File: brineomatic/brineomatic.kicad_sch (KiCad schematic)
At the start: 9 parts, among them U1 ESP32-S3-DEVKITC

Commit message: first pass fully routed
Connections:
- net +3.3V: no longer R17.2
- net GND: now also R17.2
- net Piezo/PIEZO: now also U1.20 (GPIO14); no longer U1.10 (GPIO17)
- net Servos/SERVO1: now also U1.36 (GPIO39); no longer U1.34 (GPIO37)
- net Servos/SERVO2: now also U1.34 (GPIO37); no longer U1.36 (GPIO39)
- net Stepper Driver/DIAG: now also U1.39 (GPIO42); no longer U1.38 (GPIO41)
- net Stepper Driver/DIR: now also U1.41 (GPIO1); no longer U1.40 (GPIO2)
- net Stepper Driver/EN: now also U1.38 (GPIO41); no longer U1.39 (GPIO42)
- net Stepper Driver/STEP: now also U1.40 (GPIO2); no longer U1.41 (GPIO1)
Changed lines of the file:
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@@
 	)
 	(junction
+		(at 270.51 53.34)
+		(diameter 0)
+		(color 0 0 0 0)
+	)
+	(junction
 		(at 180.34 114.3)
 		(diameter 0)
@@
 	)
 	(no_connect
-		(at 161.29 99.06)
-	)
-	(no_connect
 		(at 161.29 88.9)
 	)
@@
 	)
 	(no_connect
+		(at 161.29 76.2)
+	)
+	(no_connect
 		(at 161.29 58.42)
 	)
@@
 	(wire
 		(pts
-			(xy 209.55 43.18) (xy 237.49 43.18)
+			(xy 214.63 48.26) (xy 237.49 48.26)
 		)
 		(stroke
@@
 	(wire
 		(pts
-			(xy 59.69 78.74) (xy 64.77 78.74)
+			(xy 135.89 105.41) (xy 130.81 105.41)
 		)
 		(stroke
@@
 	(wire
 		(pts
-			(xy 33.02 162.56) (xy 39.37 162.56)
+			(xy 59.69 78.74) (xy 64.77 78.74)
 		)
 		(stroke
@@
 	(wire
 		(pts
-			(xy 199.39 78.74) (xy 214.63 78.74)
+			(xy 33.02 162.56) (xy 39.37 162.56)
 		)
 		(stroke
@@
 	(wire
 		(pts
-			(xy 257.81 53.34) (xy 261.62 53.34)
+			(xy 199.39 78.74) (xy 214.63 78.74)
 		)
 		(stroke
@@
 	(wire
 		(pts
-			(xy 201.93 104.14) (xy 199.39 104.14)
+			(xy 257.81 53.34) (xy 261.62 53.34)
 		)
 		(stroke
@@
 	(wire
 		(pts
-			(xy 214.63 48.26) (xy 237.49 48.26)
+			(xy 201.93 104.14) (xy 199.39 104.14)
 		)
 		(stroke
@@
 	(wire
 		(pts
-			(xy 130.81 73.66) (xy 161.29 73.66)
+			(xy 217.17 76.2) (xy 217.17 74.93)
 		)
 		(stroke
@@
 	(wire
 		(pts
-			(xy 217.17 76.2) (xy 217.17 74.93)
+			(xy 180.34 118.11) (xy 180.34 114.3)
 		)
 		(stroke
@@
 	(wire
 		(pts
-			(xy 180.34 118.11) (xy 180.34 114.3)
+			(xy 201.93 101.6) (xy 201.93 104.14)
 		)
 		(stroke
@@
 	(wire
 		(pts
-			(xy 201.93 101.6) (xy 201.93 104.14)
+			(xy 39.37 152.4) (xy 39.37 162.56)
 		)
 		(stroke
@@
 	(wire
 		(pts
-			(xy 39.37 152.4) (xy 39.37 162.56)
+			(xy 135.89 99.06) (xy 135.89 105.41)
 		)
 		(stroke
@@
 	(wire
 		(pts
-			(xy 212.09 45.72) (xy 237.49 45.72)
+			(xy 214.63 88.9) (xy 214.63 92.71)
 		)
 		(stroke
@@
 	(wire
 		(pts
-			(xy 214.63 88.9) (xy 214.63 92.71)
+			(xy 157.48 68.58) (xy 161.29 68.58)
 		)
 		(stroke
@@
 	(wire
 		(pts
-			(xy 157.48 68.58) (xy 161.29 68.58)
+			(xy 212.09 45.72) (xy 237.49 45.72)
 		)
 		(stroke
@@
 	(wire
 		(pts
-			(xy 217.17 52.07) (xy 237.49 52.07)
-		)
-		(stroke
-			(width 0)
-			(type default)
-		)
-	)
-	(wire
-		(pts
 			(xy 209.55 58.42) (xy 209.55 43.18)
 		)
@@
 	(wire
 		(pts
-			(xy 217.17 52.07) (xy 217.17 66.04)
+			(xy 217.17 50.8) (xy 217.17 66.04)
 		)
 		(stroke
@@
 	(wire
 		(pts
-			(xy 130.81 97.79) (xy 132.08 97.79)
+			(xy 217.17 50.8) (xy 237.49 50.8)
 		)
 		(stroke
@@
 	(wire
 		(pts
-			(xy 33.02 130.81) (xy 39.37 130.81)
+			(xy 130.81 97.79) (xy 132.08 97.79)
 		)
 		(stroke
@@
 	(wire
 		(pts
-			(xy 39.37 142.24) (xy 39.37 152.4)
+			(xy 33.02 130.81) (xy 39.37 130.81)
 		)
 		(stroke
@@
 	(wire
 		(pts
-			(xy 270.51 41.91) (xy 270.51 44.45)
+			(xy 39.37 142.24) (xy 39.37 152.4)
 		)
 		(stroke
@@
 	(wire
 		(pts
+			(xy 209.55 43.18) (xy 237.49 43.18)
+		)
+		(stroke
+			(width 0)
+			(type default)
+		)
+	)
+	(wire
+		(pts
+			(xy 161.29 99.06) (xy 135.89 99.06)
+		)
+		(stroke
+			(width 0)
+			(type default)
+		)
+	)
+	(wire
+		(pts
 			(xy 39.37 130.81) (xy 39.37 142.24)
 		)
@@
 		)
 	)
+	(wire
+		(pts
+			(xy 270.51 44.45) (xy 270.51 53.34)
+		)
+		(stroke
+			(width 0)
+			(type default)
+		)
+	)
 	(global_label "ADC_ALERT{slash}RDY"
 		(shape input)
@@
 	)
 	(symbol
-		(lib_id "power:+3.3V")
-		(at 270.51 41.91 0)
-		(unit 1)
-		(exclude_from_sim no)
-		(in_bom yes)
-		(on_board yes)
-		(dnp no)
-		(fields_autoplaced yes)
-		(property "Reference" "#PWR046"
-			(at 270.51 45.72 0)
-			(effects
-				(font
-					(size 1.27 1.27)
-				)
-				(hide yes)
-			)
-		)
-		(property "Value" "+3.3V"
-			(at 273.05 40.6399 0)
-			(effects
-				(font
-					(size 1.27 1.27)
-				)
-				(justify left)
-			)
-		)
-		(property "Footprint" ""
-			(at 270.51 41.91 0)
-			(effects
-				(font
-					(size 1.27 1.27)
-				)
-				(hide yes)
-			)
-		)
-		(property "Datasheet" ""
-			(at 270.51 41.91 0)
-			(effects
-				(font
-					(size 1.27 1.27)
-				)
-				(hide yes)
-			)
-		)
-		(property "Description" "Power symbol creates a global label with name \"+3.3V\""
-			(at 270.51 41.91 0)
-			(effects
-				(font
-					(size 1.27 1.27)
-				)
-				(hide yes)
-			)
-		)
-		(pin "1"
-		)
-		(instances
-			(project "brineomatic"
-				(path "/96477ae2-ef08-48f3-8dd4-fe4478541f68"
-					(reference "#PWR046")
-					(unit 1)
-				)
-			)
-		)
-	)
-	(symbol
 		(lib_id "power:GND")
 		(at 270.51 55.88 0)
@@
 		)
 		(pin "SERVO1" input
-			(at 222.25 74.93 180)
+			(at 222.25 72.39 180)
 			(effects
 				(font
@@
 		)
 		(pin "SERVO2" input
-			(at 222.25 72.39 180)
+			(at 222.25 74.93 180)
 			(effects
 				(font
@@
 		)
 		(pin "DIR" input
-			(at 237.49 45.72 180)
+			(at 237.49 43.18 180)
 			(effects
 				(font
@@
 		)
 		(pin "EN" input
-			(at 237.49 48.26 180)
+			(at 237.49 50.8 180)
 			(effects
 				(font
@@
 		)
 		(pin "STEP" input
-			(at 237.49 43.18 180)
+			(at 237.49 45.72 180)
 			(effects
 				(font
@@
 		)
 		(pin "DIAG" input
-			(at 237.49 52.07 180)
+			(at 237.49 48.26 180)
 			(effects
 				(font
@@
 	)
 	(sheet
-		(at 111.76 71.12)
-		(size 19.05 3.81)
-		(exclude_from_sim no)
-		(in_bom yes)
-		(on_board yes)
-		(dnp no)
-		(fields_autoplaced yes)
-		(stroke
-			(width 0.1524)
-			(type solid)
-		)
-		(fill
-			(color 0 0 0 0.0000)
-		)
-		(property "Sheetname" "Piezo"
-			(at 111.76 70.4084 0)
-			(effects
-				(font
-					(size 1.27 1.27)
-				)
-				(justify left bottom)
-			)
-		)
-		(property "Sheetfile" "piezo.kicad_sch"
-			(at 111.76 75.5146 0)
-			(effects
-				(font
-					(size 1.27 1.27)
-				)
-				(justify left top)
-				(hide yes)
-			)
-		)
-		(pin "PIEZO" input
-			(at 130.81 73.66 0)
-			(effects
-				(font
-					(size 1.27 1.27)
-				)
-				(justify right)
-			)
-		)
-		(instances
-			(project "brineomatic"
-				(path "/96477ae2-ef08-48f3-8dd4-fe4478541f68"
-					(page "16")
-				)
-			)
-		)
-	)
-	(sheet
 		(at 222.25 107.95)
 		(size 31.75 5.08)
@@
 				)
 			)
+		)
+	)
+	(sheet
+		(at 111.76 102.87)
+		(size 19.05 3.81)
+		(exclude_from_sim no)
+		(in_bom yes)
+		(on_board yes)
+		(dnp no)
+		(fields_autoplaced yes)
+		(stroke
+			(width 0.1524)
+			(type solid)
+		)
+		(fill
+			(color 0 0 0 0.0000)
+		)
+		(property "Sheetname" "Piezo"
+			(at 111.76 102.1584 0)
+			(effects
+				(font
+					(size 1.27 1.27)
+				)
+				(justify left bottom)
+			)
+		)
+		(property "Sheetfile" "piezo.kicad_sch"
+			(at 111.76 107.2646 0)
+			(effects
+				(font
+					(size 1.27 1.27)
+				)
+				(justify left top)
+				(hide yes)
+			)
+		)
+		(pin "PIEZO" input
+			(at 130.81 105.41 0)
+			(effects
+				(font
+					(size 1.27 1.27)
+				)
+				(justify right)
+			)
+		)
+		(instances
+			(project "brineomatic"
+				(path "/96477ae2-ef08-48f3-8dd4-fe4478541f68"
+					(page "9")
+				)
+			)

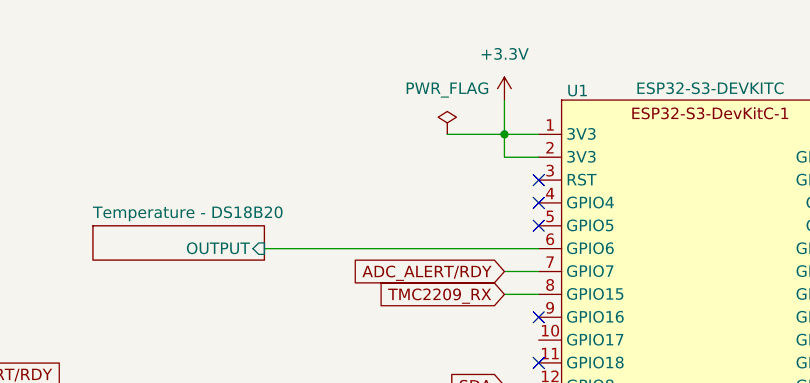
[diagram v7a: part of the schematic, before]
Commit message: added fuse on 3.3v
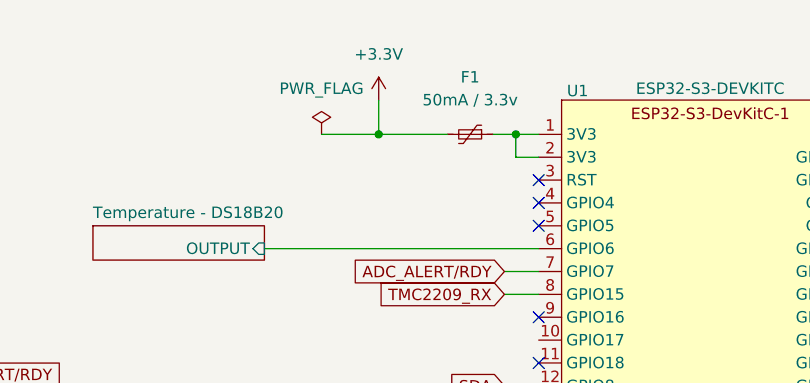
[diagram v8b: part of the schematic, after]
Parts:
- added F1: 50mA / 3.3v, Fuse:Fuse_0603_1608Metric, symbol Device:Polyfuse_Small
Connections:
- net +3.3V: now also F1.2; no longer U1.1 (3V3), U1.2 (3V3)
- new net: F1.1, U1.1 (3V3), U1.2 (3V3)
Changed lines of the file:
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@@
+	)
+	(junction
+		(at 158.75 50.8)
+		(diameter 0)
+		(color 0 0 0 0)
 	)
 	(junction
@@
 	)
 	(junction
-		(at 157.48 50.8)
+		(at 143.51 50.8)
 		(diameter 0)
 		(color 0 0 0 0)
@@
 	(wire
 		(pts
-			(xy 151.13 50.8) (xy 157.48 50.8)
+			(xy 137.16 50.8) (xy 143.51 50.8)
 		)
 		(stroke
@@
 	(wire
 		(pts
-			(xy 161.29 53.34) (xy 157.48 53.34)
-		)
-		(stroke
-			(width 0)
-			(type default)
-		)
-	)
-	(wire
-		(pts
 			(xy 62.23 73.66) (xy 62.23 59.69)
 		)
@@
 	(wire
 		(pts
+			(xy 156.21 50.8) (xy 158.75 50.8)
+		)
+		(stroke
+			(width 0)
+			(type default)
+		)
+	)
+	(wire
+		(pts
 			(xy 214.63 63.5) (xy 214.63 48.26)
 		)
@@
 	(wire
 		(pts
+			(xy 158.75 53.34) (xy 158.75 50.8)
+		)
+		(stroke
+			(width 0)
+			(type default)
+		)
+	)
+	(wire
+		(pts
 			(xy 257.81 53.34) (xy 261.62 53.34)
 		)
@@
 	(wire
 		(pts
+			(xy 158.75 50.8) (xy 161.29 50.8)
+		)
+		(stroke
+			(width 0)
+			(type default)
+		)
+	)
+	(wire
+		(pts
 			(xy 93.98 74.93) (xy 93.98 68.58)
 		)
@@
 	(wire
 		(pts
-			(xy 157.48 50.8) (xy 157.48 53.34)
-		)
-		(stroke
-			(width 0)
-			(type default)
-		)
-	)
-	(wire
-		(pts
 			(xy 217.17 72.39) (xy 217.17 71.12)
 		)
@@
 	(wire
 		(pts
-			(xy 157.48 46.99) (xy 157.48 50.8)
+			(xy 143.51 46.99) (xy 143.51 50.8)
 		)
 		(stroke
@@
 	(wire
 		(pts
-			(xy 157.48 50.8) (xy 161.29 50.8)
+			(xy 143.51 50.8) (xy 151.13 50.8)
 		)
 		(stroke
@@
 		(pts
 			(xy 158.75 104.14) (xy 158.75 114.3)
+		)
+		(stroke
+			(width 0)
+			(type default)
+		)
+	)
+	(wire
+		(pts
+			(xy 161.29 53.34) (xy 158.75 53.34)
 		)
 		(stroke
@@
 	(symbol
 		(lib_id "power:+3.3V")
-		(at 157.48 46.99 0)
+		(at 143.51 46.99 0)
 		(unit 1)
 		(exclude_from_sim no)
@@
 		(fields_autoplaced yes)
 		(property "Reference" "#PWR03"
-			(at 157.48 50.8 0)
+			(at 143.51 50.8 0)
 			(effects
 				(font
@@
 		)
 		(property "Value" "+3.3V"
-			(at 157.48 41.91 0)
+			(at 143.51 41.91 0)
 			(effects
 				(font
@@
 		)
 		(property "Footprint" ""
-			(at 157.48 46.99 0)
+			(at 143.51 46.99 0)
 			(effects
 				(font
@@
 		)
 		(property "Datasheet" ""
-			(at 157.48 46.99 0)
+			(at 143.51 46.99 0)
 			(effects
 				(font
@@
 		)
 		(property "Description" "Power symbol creates a global label with name \"+3.3V\""
-			(at 157.48 46.99 0)
+			(at 143.51 46.99 0)
 			(effects
 				(font
@@
 				(path "/96477ae2-ef08-48f3-8dd4-fe4478541f68"
 					(reference "H3")
+					(unit 1)
+				)
+			)
+		)
+	)
+	(symbol
+		(lib_id "Device:Polyfuse_Small")
+		(at 153.67 50.8 270)
+		(unit 1)
+		(exclude_from_sim no)
+		(in_bom yes)
+		(on_board yes)
+		(dnp no)
+		(fields_autoplaced yes)
+		(property "Reference" "F1"
+			(at 153.67 44.45 90)
+			(effects
+				(font
+					(size 1.27 1.27)
+				)
+			)
+		)
+		(property "Value" "50mA / 3.3v"
+			(at 153.67 46.99 90)
+			(effects
+				(font
+					(size 1.27 1.27)
+				)
+			)
+		)
+		(property "Footprint" "Fuse:Fuse_0603_1608Metric"
+			(at 148.59 52.07 0)
+			(effects
+				(font
+					(size 1.27 1.27)
+				)
+				(justify left)
+				(hide yes)
+			)
+		)
+		(property "Datasheet" "~"
+			(at 153.67 50.8 0)
+			(effects
+				(font
+					(size 1.27 1.27)
+				)
+				(hide yes)
+			)
+		)
+		(property "Description" ""
+			(at 153.67 50.8 0)
+			(effects
+				(font
+					(size 1.27 1.27)
+				)
+				(hide yes)
+			)
+		)
+		(property "LCSC" ""
+			(at 153.67 50.8 90)
+			(effects
+				(font
+					(size 1.27 1.27)
+				)
+				(hide yes)
+			)
+		)
+		(pin "1"
+		)
+		(pin "2"
+		)
+		(instances
+			(project "brineomatic"
+				(path "/96477ae2-ef08-48f3-8dd4-fe4478541f68"
+					(reference "F1")
 					(unit 1)
 				)
@@
 	(symbol
 		(lib_id "power:PWR_FLAG")
-		(at 151.13 50.8 0)
+		(at 137.16 50.8 0)
 		(unit 1)
 		(exclude_from_sim no)
@@
 		(fields_autoplaced yes)
 		(property "Reference" "#FLG01"
-			(at 151.13 48.895 0)
+			(at 137.16 48.895 0)
 			(effects
 				(font
@@
 		)
 		(property "Value" "PWR_FLAG"
-			(at 151.13 45.72 0)
+			(at 137.16 45.72 0)
 			(effects
 				(font
@@
 		)
 		(property "Footprint" ""
-			(at 151.13 50.8 0)
+			(at 137.16 50.8 0)
 			(effects
 				(font
@@
 		)
 		(property "Datasheet" "~"
-			(at 151.13 50.8 0)
+			(at 137.16 50.8 0)
 			(effects
 				(font
@@
 		)
 		(property "Description" "Special symbol for telling ERC where power comes from"
-			(at 151.13 50.8 0)
-			(effects
-				(font
+			(at 137.16 50.8 0)
+			(effects
+				(font
